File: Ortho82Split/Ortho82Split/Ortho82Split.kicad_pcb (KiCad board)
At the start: 2 copper layers, 155.4 x 123.1 mm, 109 parts, among them J3 USB_C_Receptacle_USB2.0, J6 Conn_01x06_Socket, J7 Conn_01x08_Socket, J8 Conn_01x06_Socket, J9 TC2030-IDC-NL, SW11 SW_Push, SW12 SW_Push, SW13 SW_Push, SW14 SW_Push, SW15 SW_Push, SW16 SW_Push, SW17 SW_Push, SW18 SW_Push, SW19 SW_Push, SW20 SW_Push, SW21 SW_Push, SW22 SW_Push, SW23 SW_Push, SW24 SW_Push, SW25 SW_Push, SW26 SW_Push, SW27 SW_Push, SW28 SW_Push, SW29 SW_Push, SW30 SW_Push, SW31 SW_Push, SW32 SW_Push, SW33 SW_Push, SW34 SW_Push, SW35 SW_Push, SW36 SW_Push, SW37 SW_Push, SW38 SW_Push, SW39 SW_Push, SW40 SW_Push, SW41 SW_Push, SW42 SW_Push, SW43 SW_Push, SW44 SW_Push, SW45 SW_Push, SW46 SW_Push, SW47 SW_Push, SW48 SW_Push, SW49 SW_Push, SW50 SW_Push, SW51 SW_Push, SW74 OS, SW83 SW_Push, U1 MCP1700T-3302E_TT, U2 ATxmega32A4U-A, U3 USBLC6-2SC6

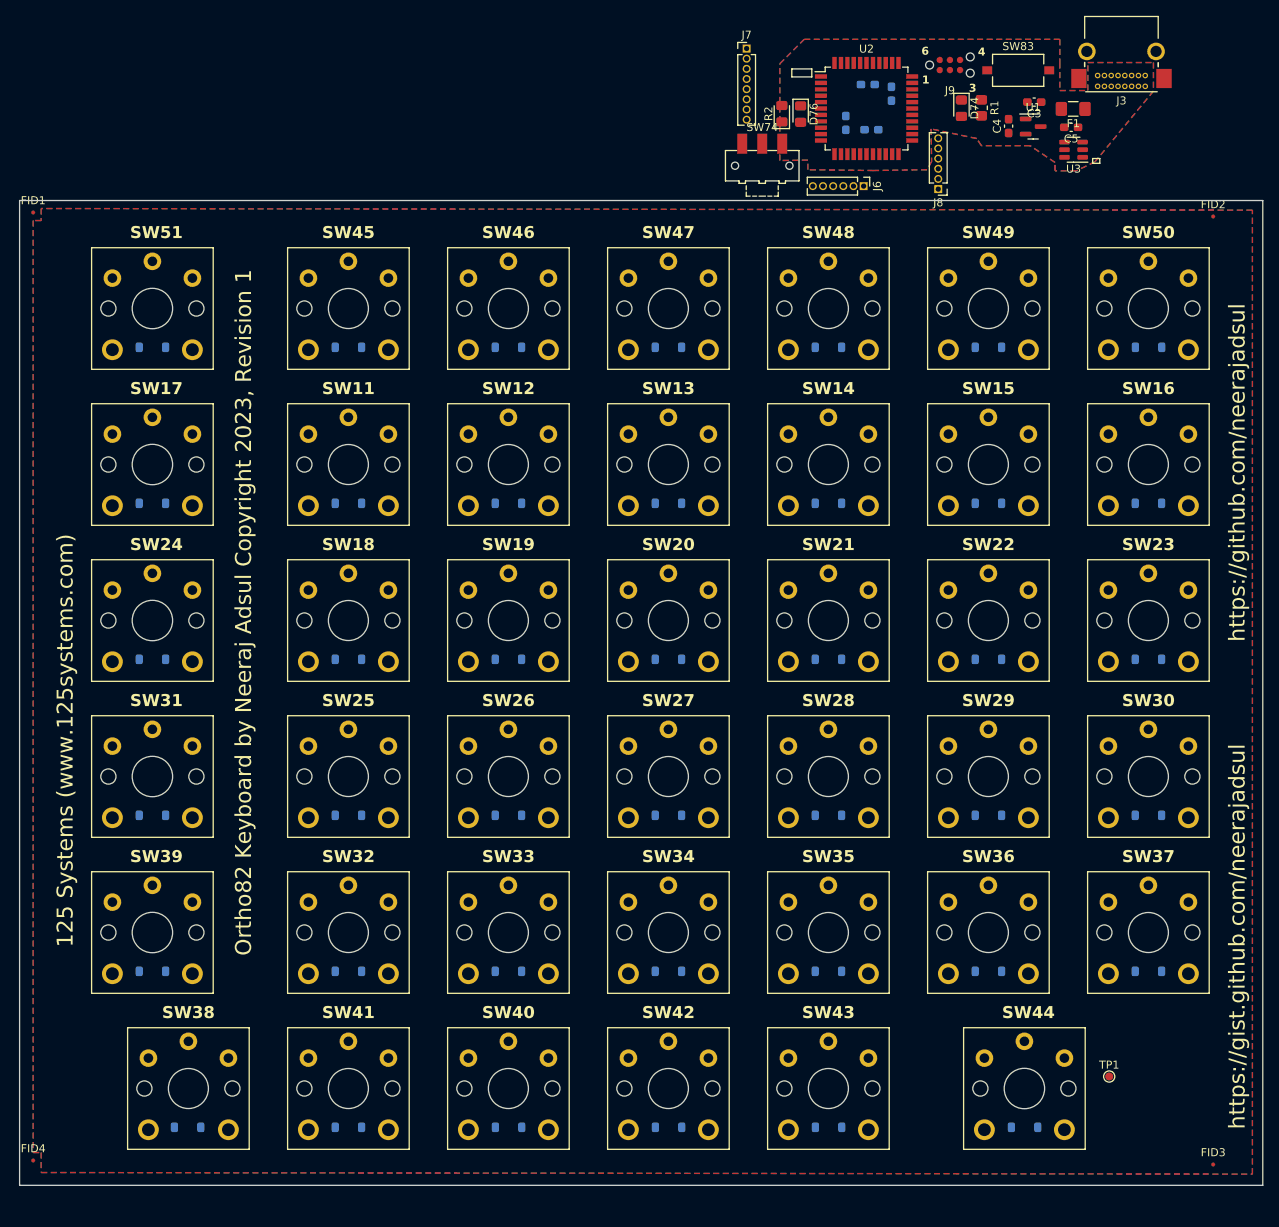
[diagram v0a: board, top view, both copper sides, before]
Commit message: Corrects spacing between keyswitches.
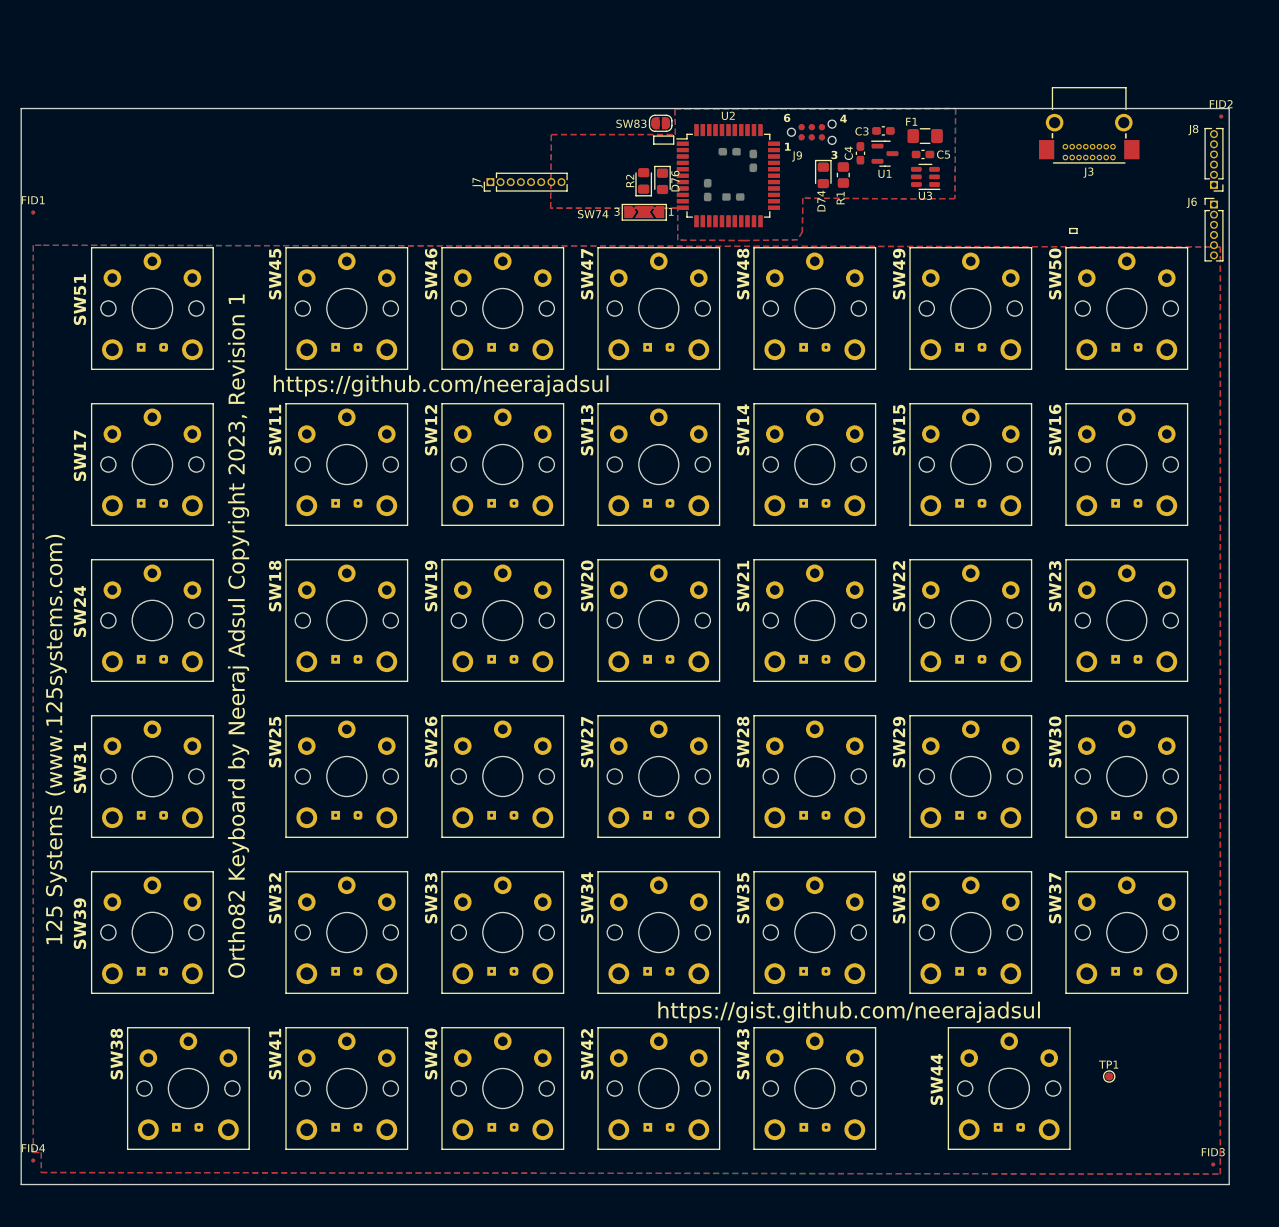
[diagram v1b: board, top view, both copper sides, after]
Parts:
- D11, D12, D13, D14, D15, D16, D17, D18, D19, D20, D21, D22, D23, D24, D25, D26, D27, D28, D29, D30, D31, D32, D33, D34, D35, D36, D37, D38, D39, D40, D41, D42, D43, D44, D45, D46, D47, D48, D49, D50, D51: footprint Diode_SMD:D_SOD-123 -> HandsolderModifiedComponents:D_SOD-123F_DoubleSided
- SW74: value OS -> Left/Right; footprint Button_Switch_SMD:SW_SPDT_CK-JS102011SAQN -> Jumper:SolderJumper-3_P2.0mm_Open_TrianglePad1.0x1.5mm_NumberLabels
- SW83: value SW_Push -> ~{RESET}; footprint Button_Switch_SMD:SW_Tactile_SPST_NO_Straight_CK_PTS636Sx25SMTRLFS -> Jumper:SolderJumper-2_P1.3mm_Open_RoundedPad1.0x1.5mm
- moved SW83 45.2 mm to (118.9, 41.8), turned to 180 degrees
- moved J6 43.9 mm to (188.1, 52.0), turned to 0 degrees
- moved J7 36.1 mm to (97.7, 49.2), turned to 90 degrees
- moved J8 34.5 mm to (188.1, 49.5)
- moved C1 19.2 mm to (124.8, 50.2)
- moved C2 19.2 mm to (130.5, 46.5)
- moved C6 19.2 mm to (128.0, 51.0)
- moved C7 19.2 mm to (127.6, 45.4)
- moved D74 19.2 mm to (139.3, 48.4)
- moved D76 19.2 mm to (119.2, 49.1)
- moved J9 19.2 mm to (137.8, 43.0)
- moved R1 19.2 mm to (141.8, 48.3)
- moved R2 19.2 mm to (116.8, 49.0)
- moved U2 19.2 mm to (127.4, 48.4)
- moved C3 19.2 mm to (146.8, 42.8)
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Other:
- board size 155.4 x 123.1 mm -> 151 x 134.5 mm

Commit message: Route USB and xmega circuit.
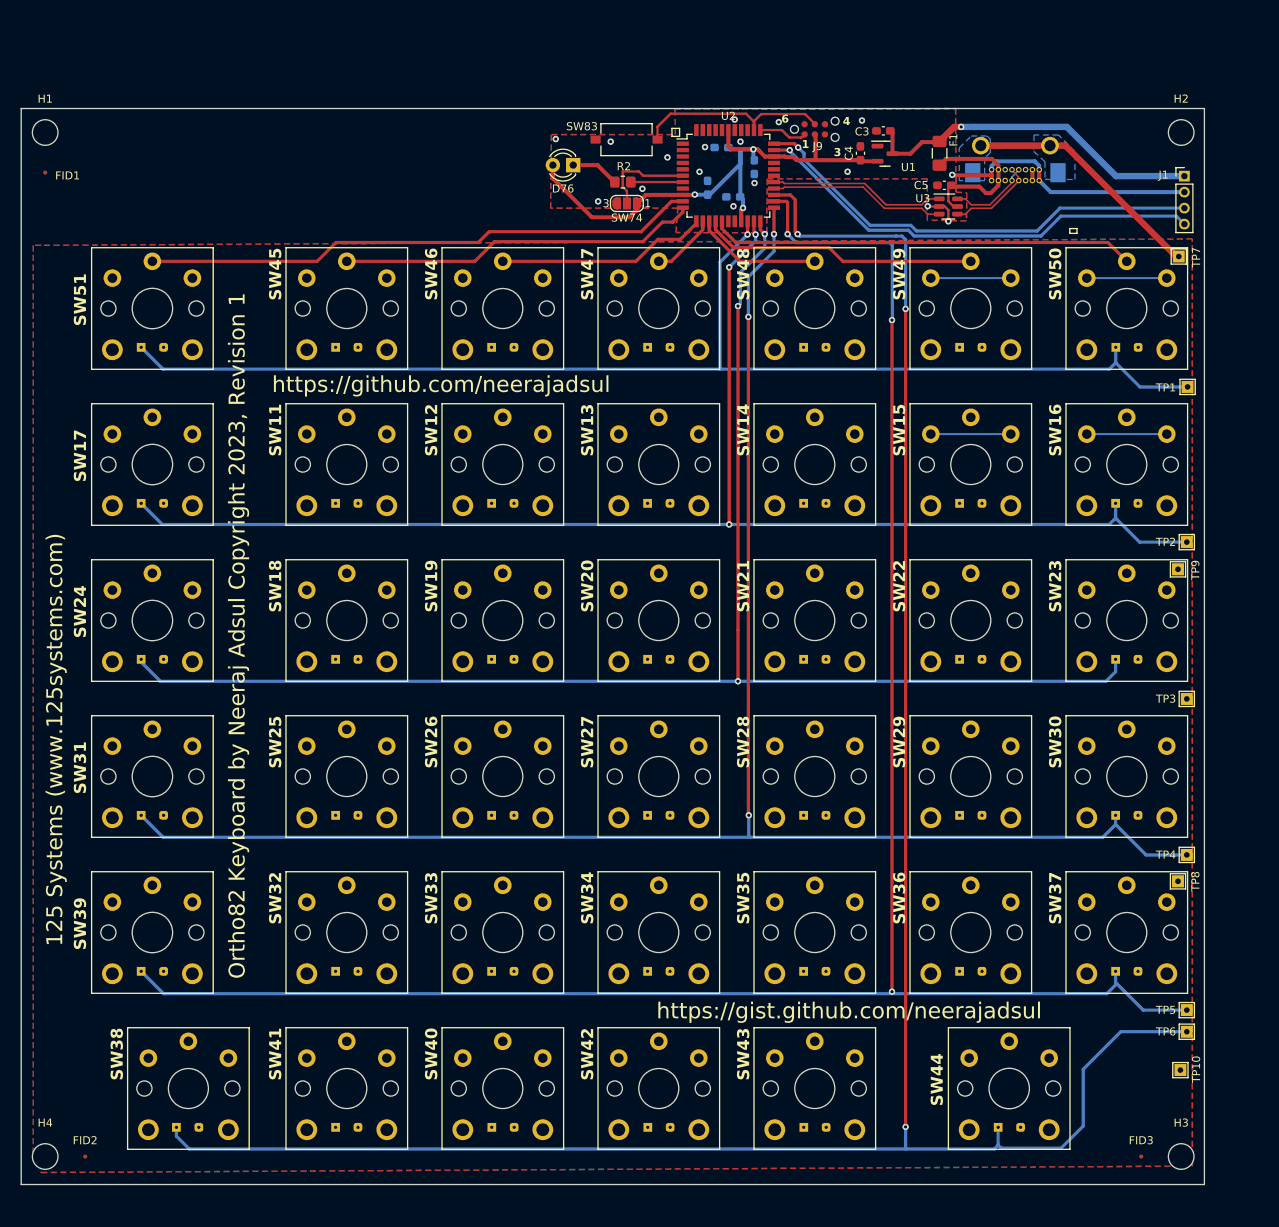
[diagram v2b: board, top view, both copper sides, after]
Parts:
- removed D74: Green, LED_SMD:LED_0805_2012Metric_Pad1.15x1.40mm_HandSolder
- removed the FID2 at (189.0, 41.0)
- removed J6, J8: Conn_01x06_Socket, Connector_PinHeader_1.27mm:PinHeader_1x06_P1.27mm_Vertical
- removed J7: Conn_01x08_Socket, Connector_PinHeader_1.27mm:PinHeader_1x08_P1.27mm_Vertical
- removed R1: 499, Resistor_SMD:R_0805_2012Metric_Pad1.20x1.40mm_HandSolder
- added H1: MountingHole, MountingHole:MountingHole_3.2mm_M3, F.Cu at (42.0, 43.0)
- added H2: MountingHole, MountingHole:MountingHole_3.2mm_M3, F.Cu at (184.0, 43.0)
- added H3: MountingHole, MountingHole:MountingHole_3.2mm_M3, F.Cu at (184.0, 171.0)
- added H4: MountingHole, MountingHole:MountingHole_3.2mm_M3, F.Cu at (42.0, 171.0)
- added J1: Left-Right, Connector_PinHeader_2.00mm:PinHeader_1x04_P2.00mm_Vertical, F.Cu at (184.4, 48.5)
- added TP10: SHIELD_POUR, TestPoint:TestPoint_THTPad_1.5x1.5mm_Drill0.7mm, F.Cu at (183.9, 160.2)
- added TP2: ROW_0, TestPoint:TestPoint_THTPad_1.5x1.5mm_Drill0.7mm, F.Cu at (184.7, 94.2)
- added TP3: ROW_1, TestPoint:TestPoint_THTPad_1.5x1.5mm_Drill0.7mm, F.Cu at (184.7, 113.8)
- added TP4: ROW_2, TestPoint:TestPoint_THTPad_1.5x1.5mm_Drill0.7mm, F.Cu at (184.7, 133.3)
- added TP5: ROW_3, TestPoint:TestPoint_THTPad_1.5x1.5mm_Drill0.7mm, F.Cu at (184.7, 152.7)
- added TP6: ROW_4, TestPoint:TestPoint_THTPad_1.5x1.5mm_Drill0.7mm, F.Cu at (184.7, 155.4)
- added TP7: SHIELD_POUR, TestPoint:TestPoint_THTPad_1.5x1.5mm_Drill0.7mm, F.Cu at (183.7, 58.5)
- added TP8: SHIELD_POUR, TestPoint:TestPoint_THTPad_1.5x1.5mm_Drill0.7mm, F.Cu at (183.6, 136.6)
- added TP9: SHIELD_POUR, TestPoint:TestPoint_THTPad_1.5x1.5mm_Drill0.7mm, F.Cu at (183.6, 97.6)
- D76: footprint LED_SMD:LED_0805_2012Metric_Pad1.15x1.40mm_HandSolder -> LED_THT:LED_D3.0mm
- J3: moved to B.Cu
- R2: footprint LED_SMD:LED_0805_2012Metric_Pad1.15x1.40mm_HandSolder -> Resistor_SMD:R_0805_2012Metric_Pad1.20x1.40mm_HandSolder
- SW74: footprint Jumper:SolderJumper-3_P2.0mm_Open_TrianglePad1.0x1.5mm_NumberLabels -> Jumper:SolderJumper-3_P1.3mm_Open_RoundedPad1.0x1.5mm_NumberLabels
- SW83: footprint Jumper:SolderJumper-2_P1.3mm_Open_RoundedPad1.0x1.5mm -> Button_Switch_SMD:SW_Tactile_SPST_NO_Straight_CK_PTS636Sx25SMTRLFS
- TP1: value TestPoint -> ROW_F; footprint TestPoint:TestPoint_Pad_D1.0mm -> TestPoint:TestPoint_THTPad_1.5x1.5mm_Drill0.7mm
- moved TP1 86.8 mm to (184.8, 74.8)
- moved J3 15.4 mm to (160.3, 49.0), turned to 0 degrees
- moved D76 11.3 mm to (108.0, 47.1), turned to 180 degrees
- moved FID3 9.06 mm to (179.0, 171.0)
- moved FID2 6.52 mm to (47.0, 171.0)
- moved FID1 5.22 mm to (42.0, 48.0)
- moved SW83 4.74 mm to (114.7, 43.9)
- moved C5 4.69 mm to (154.4, 49.6)
- moved U3 4.69 mm to (154.9, 52.2), turned to 0 degrees
- moved F1 2.82 mm to (153.8, 45.6), turned to 90 degrees
- moved R2 2.62 mm to (114.2, 49.2), turned to 180 degrees
- moved SW74 2.43 mm to (114.7, 51.9)
- moved C7 1.16 mm to (126.5, 44.9), turned to 180 degrees
- moved C2 0.79 mm to (130.6, 47.3)
- moved J9 0.53 mm to (138.2, 42.6)
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- renumbered FID4 to FID2
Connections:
- SW11 pad 1: /COL_0 -> /COL_1
- SW12 pad 1: /COL_1 -> /COL_2
- SW13 pad 1: /COL_2 -> /COL_3
- SW14 pad 1: /COL_3 -> /COL_4
- SW15 pad 1: /COL_4 -> /COL_5
- SW16 pad 1: /COL_5 -> /COL_6
- SW17 pad 1: /COL_6 -> /COL_0
- SW18 pad 1: /COL_0 -> /COL_1
- SW19 pad 1: /COL_1 -> /COL_2
- SW20 pad 1: /COL_2 -> /COL_3
- SW21 pad 1: /COL_3 -> /COL_4
- SW22 pad 1: /COL_4 -> /COL_5
- SW23 pad 1: /COL_5 -> /COL_6
- SW24 pad 1: /COL_6 -> /COL_0
- SW25 pad 1: /COL_0 -> /COL_1
- SW26 pad 1: /COL_1 -> /COL_2
- SW27 pad 1: /COL_2 -> /COL_3
- SW28 pad 1: /COL_3 -> /COL_4
- SW29 pad 1: /COL_4 -> /COL_5
- SW30 pad 1: /COL_5 -> /COL_6
- SW31 pad 1: /COL_6 -> /COL_0
- SW32 pad 1: /COL_0 -> /COL_1
- SW33 pad 1: /COL_1 -> /COL_2
- SW34 pad 1: /COL_2 -> /COL_3
- SW35 pad 1: /COL_3 -> /COL_4
- SW36 pad 1: /COL_4 -> /COL_5
- SW37 pad 1: /COL_5 -> /COL_6
- SW38 pad 1: /COL_0 -> /COL_1
- SW39 pad 1: /COL_6 -> /COL_0
- SW40 pad 1: /COL_2 -> /COL_3
- SW41 pad 1: /COL_1 -> /COL_2
- SW42 pad 1: /COL_3 -> /COL_4
- SW43 pad 1: /COL_4 -> /COL_5
- SW44 pad 1: /COL_5 -> /COL_6
- SW45 pad 1: /COL_0 -> /COL_1
- SW46 pad 1: unconnected-(SW46-Pad1) -> /COL_2
- SW47 pad 1: /COL_2 -> /COL_3
- SW48 pad 1: /COL_3 -> /COL_4
- SW49 pad 1: /COL_4 -> /COL_5
- SW50 pad 1: /COL_5 -> /COL_6
- SW51 pad 1: /COL_6 -> /COL_0
- TP1 pad 1: /SHIELD_POUR -> /ROW_F
- U2 pad 1: /COL_5 -> unconnected-(U2-PA5-Pad1)
- U2 pad 10: /ROW_4 -> /COL_0
- U2 pad 11: /ROW_3 -> /COL_1
- U2 pad 12: /ROW_2 -> /COL_2
- U2 pad 13: /ROW_1 -> /COL_3
- U2 pad 14: /ROW_0 -> /COL_4
- U2 pad 15: /ROW_F -> /COL_5
- U2 pad 16: unconnected-(U2-PC6-Pad16) -> /COL_6
- U2 pad 2: /COL_6 -> unconnected-(U2-PA6-Pad2)
- U2 pad 20: /COL_8 -> /ROW_F
- U2 pad 21: /COL_9 -> /ROW_0
- U2 pad 22: /COL_10 -> /ROW_1
- U2 pad 23: /COL_11 -> /ROW_2
- U2 pad 24: /COL_12 -> /ROW_3
- U2 pad 25: /COL_13 -> /ROW_4
- U2 pad 3: /COL_7 -> unconnected-(U2-PA7-Pad3)
- U2 pad 32: unconnected-(U2-PE2-Pad32) -> /RXD0
- U2 pad 33: unconnected-(U2-PE3-Pad33) -> /TXD0
- U2 pad 4: Net-(SW74-B) -> unconnected-(U2-AREFB/PB0-Pad4)
- U2 pad 40: /COL_0 -> unconnected-(U2-AREFA/PA0-Pad40)
- U2 pad 41: /COL_1 -> unconnected-(U2-PA1-Pad41)
- U2 pad 42: /COL_2 -> unconnected-(U2-PA2-Pad42)
- U2 pad 43: /COL_3 -> unconnected-(U2-PA3-Pad43)
- U2 pad 44: /COL_4 -> unconnected-(U2-PA4-Pad44)
- U2 pad 6: unconnected-(U2-PB2-Pad6) -> Net-(SW74-B)
- U3 pad 1: /USB_D+ -> /USBM+
- U3 pad 3: /USB_D- -> /USBM-
- U3 pad 4: /USBM- -> /USB_D-
- U3 pad 6: /USBM+ -> /USB_D+
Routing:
- net /ROW_4: track 0.00 -> 275.6 mm, vias 0 -> 3
- net /ROW_3: track 0.00 -> 248.2 mm, vias 0 -> 3
- net /ROW_2: track 0.00 -> 215.3 mm, vias 0 -> 3
- net /ROW_1: track 0.00 -> 184.3 mm, vias 0 -> 3
- net /ROW_0: track 0.00 -> 174.6 mm, vias 0 -> 3
- net /ROW_F: track 0.00 -> 155.4 mm, vias 0 -> 1
- net +3V3: track 0.00 -> 70.4 mm, vias 0 -> 3
- net /COL_0: track 0.00 -> 69.4 mm
- net /TXD0: track 0.00 -> 57.4 mm, vias 0 -> 1
- net /RXD0: track 0.00 -> 57.3 mm, vias 0 -> 1
- net /COL_6: track 0.00 -> 53.2 mm
- net /COL_1: track 0.00 -> 45.1 mm
- net /VBUS_FUSED: track 0.00 -> 43.4 mm, vias 0 -> 1
- net GND: track 0.00 -> 38.0 mm, vias 0 -> 17
- net /COL_5: track 0.00 -> 34.6 mm
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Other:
- board size 151 x 134.5 mm -> 147.9 x 134.5 mm

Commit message: Routing complete.
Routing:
- net /COL_5: track 34.6 -> 160.8 mm
- net /COL_1: track 45.1 -> 167.8 mm
- net /COL_2: track 26.4 -> 147.6 mm
- net /COL_4: track 15.9 -> 137.2 mm
- net /COL_3: track 8.19 -> 128.9 mm
- net /COL_6: track 53.2 -> 171.1 mm
- net /COL_0: track 69.4 -> 182.2 mm
- net /ROW_1: track 184.3 -> 208.5 mm
- net Net-(D45-A): track 0.00 -> 21.0 mm
- net Net-(D38-A): track 0.00 -> 20.2 mm
- net Net-(D34-A): track 0.00 -> 20.1 mm
- net Net-(D41-A): track 0.00 -> 20.1 mm
- net Net-(D33-A): track 0.00 -> 20.1 mm
- net Net-(D39-A): track 0.00 -> 20.1 mm
- net Net-(D36-A): track 0.00 -> 20.1 mm
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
